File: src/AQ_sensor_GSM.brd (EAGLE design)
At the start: 110.2 x 66.3 mm, 115 parts, among them J1 F-1X03-SIP-100-32, J2 53261-0871, J3 PJ-002BH, Q2 MMBT2222, Q3 MMBT2222, Q4 MMBT2222, Q5 MMBT2222, Q6 MMBT2222, Q7 MMBT2222, Q8 FS8205, U3 TEXAS_INSTRUMENTS_LM1117IMP-3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, U5 TXS0108EPWR

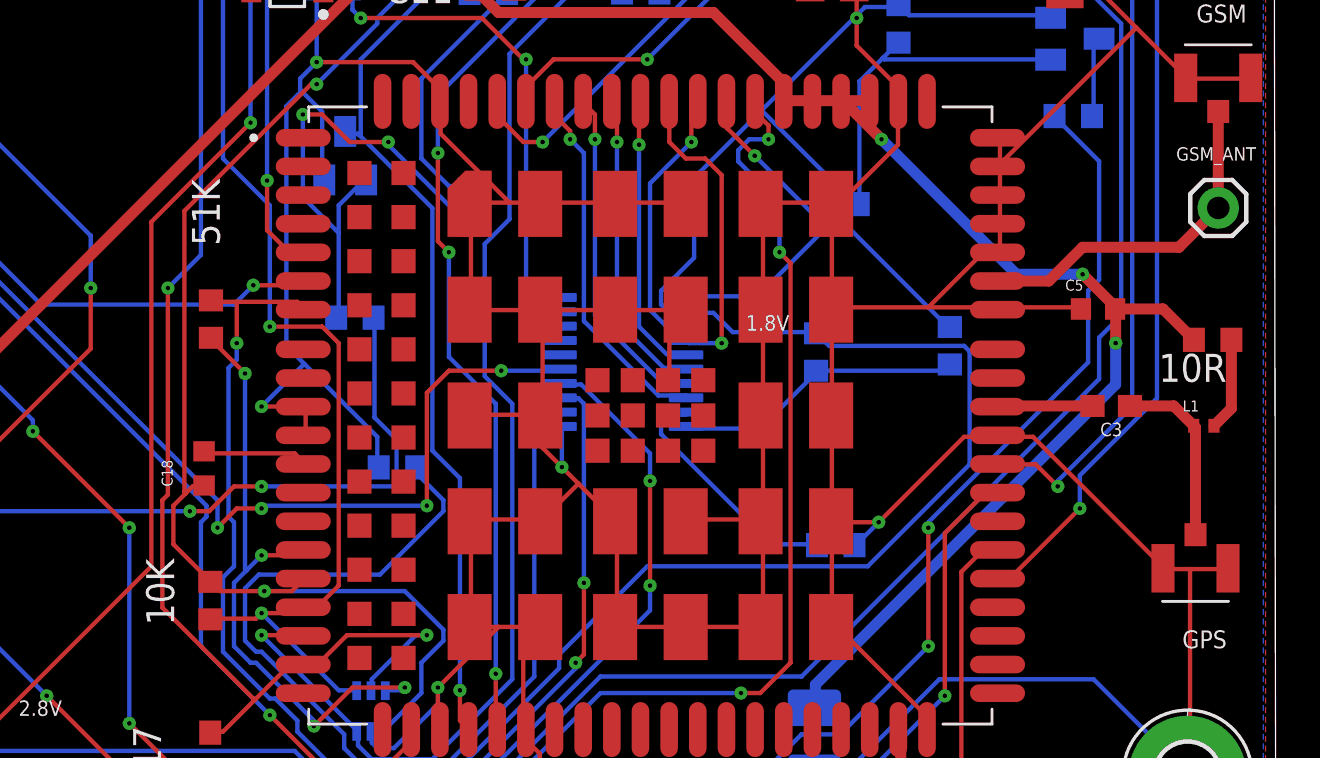
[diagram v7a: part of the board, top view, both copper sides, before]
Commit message: Nigeria Order, PCB Routed
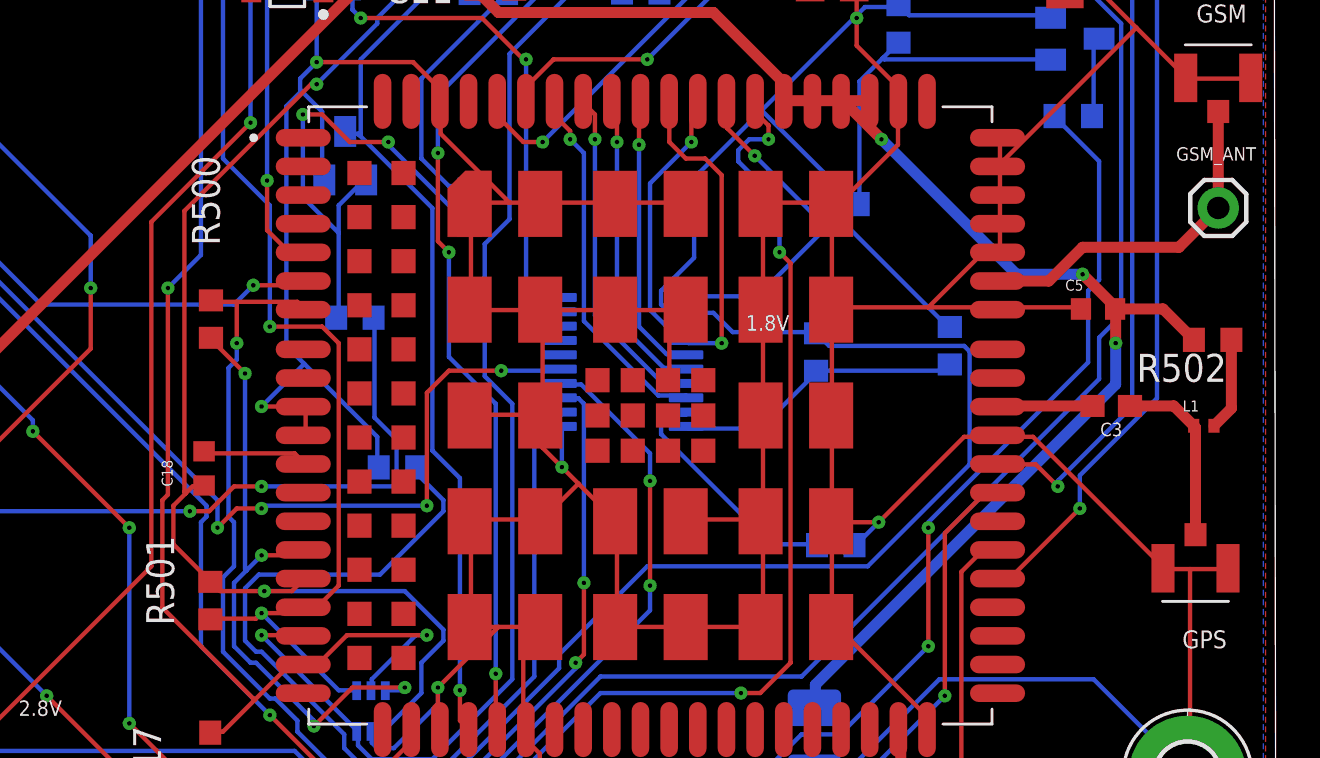
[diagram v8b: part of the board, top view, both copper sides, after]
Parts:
- renumbered 10K to R501, 10R to R502, 51K to R500
